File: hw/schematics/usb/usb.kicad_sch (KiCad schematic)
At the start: 4 parts

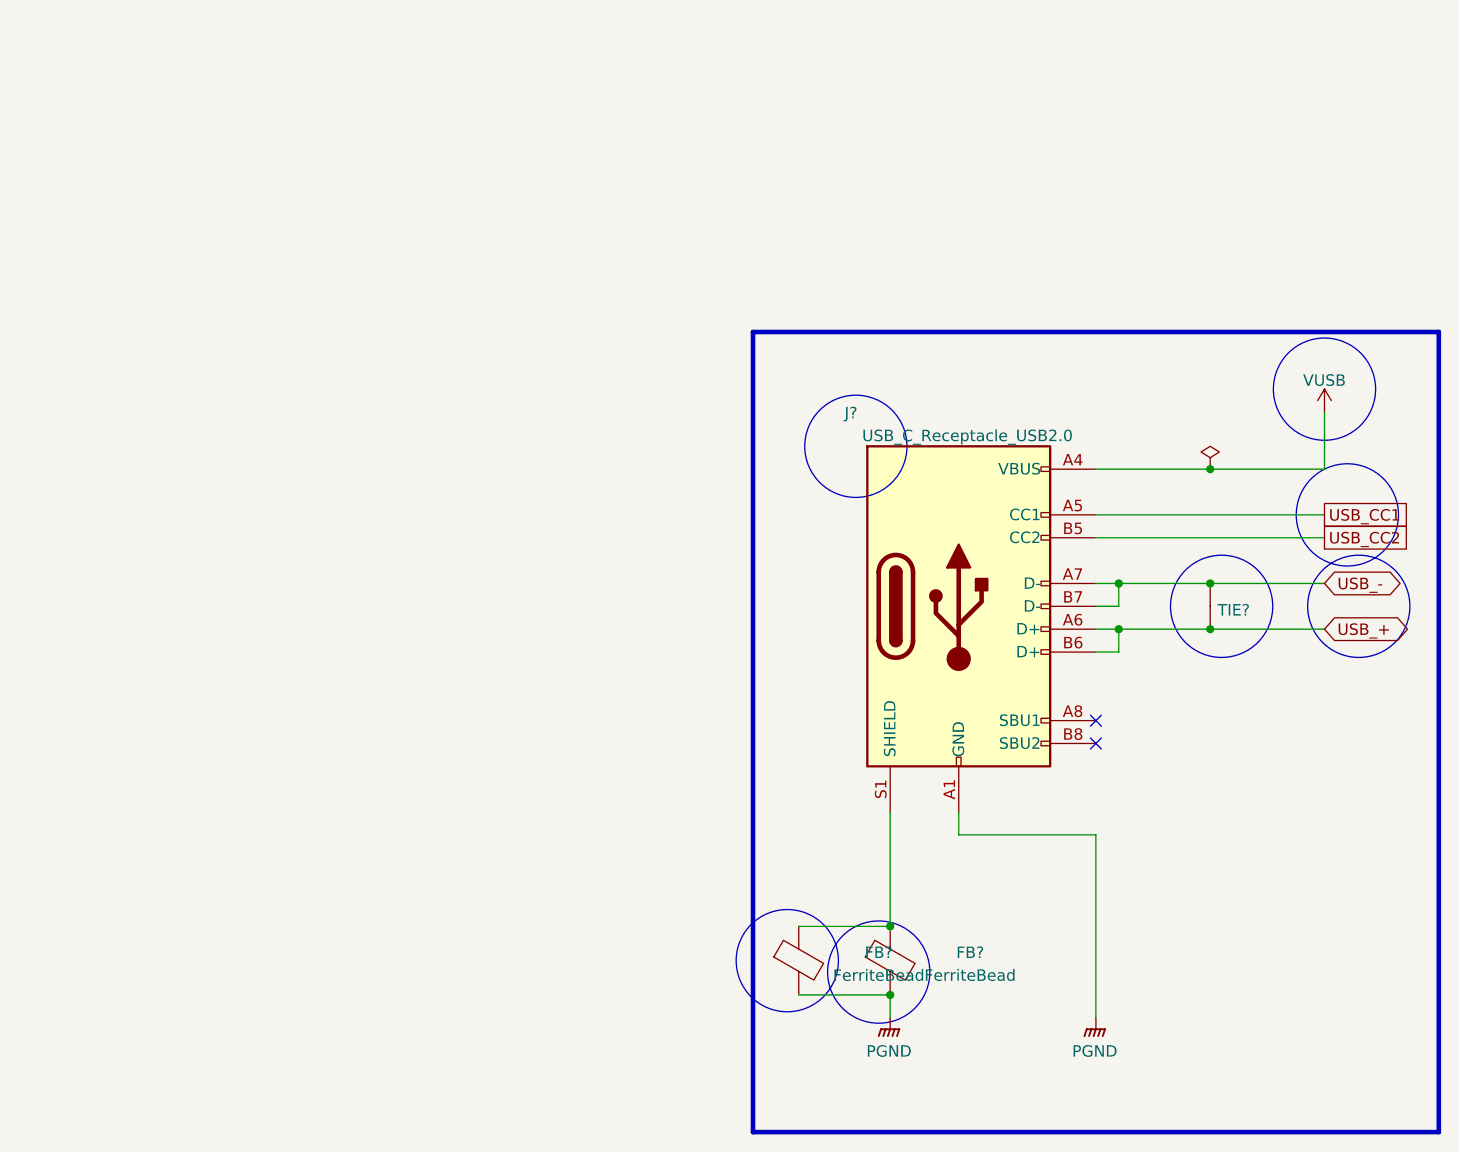
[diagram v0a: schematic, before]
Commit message: 
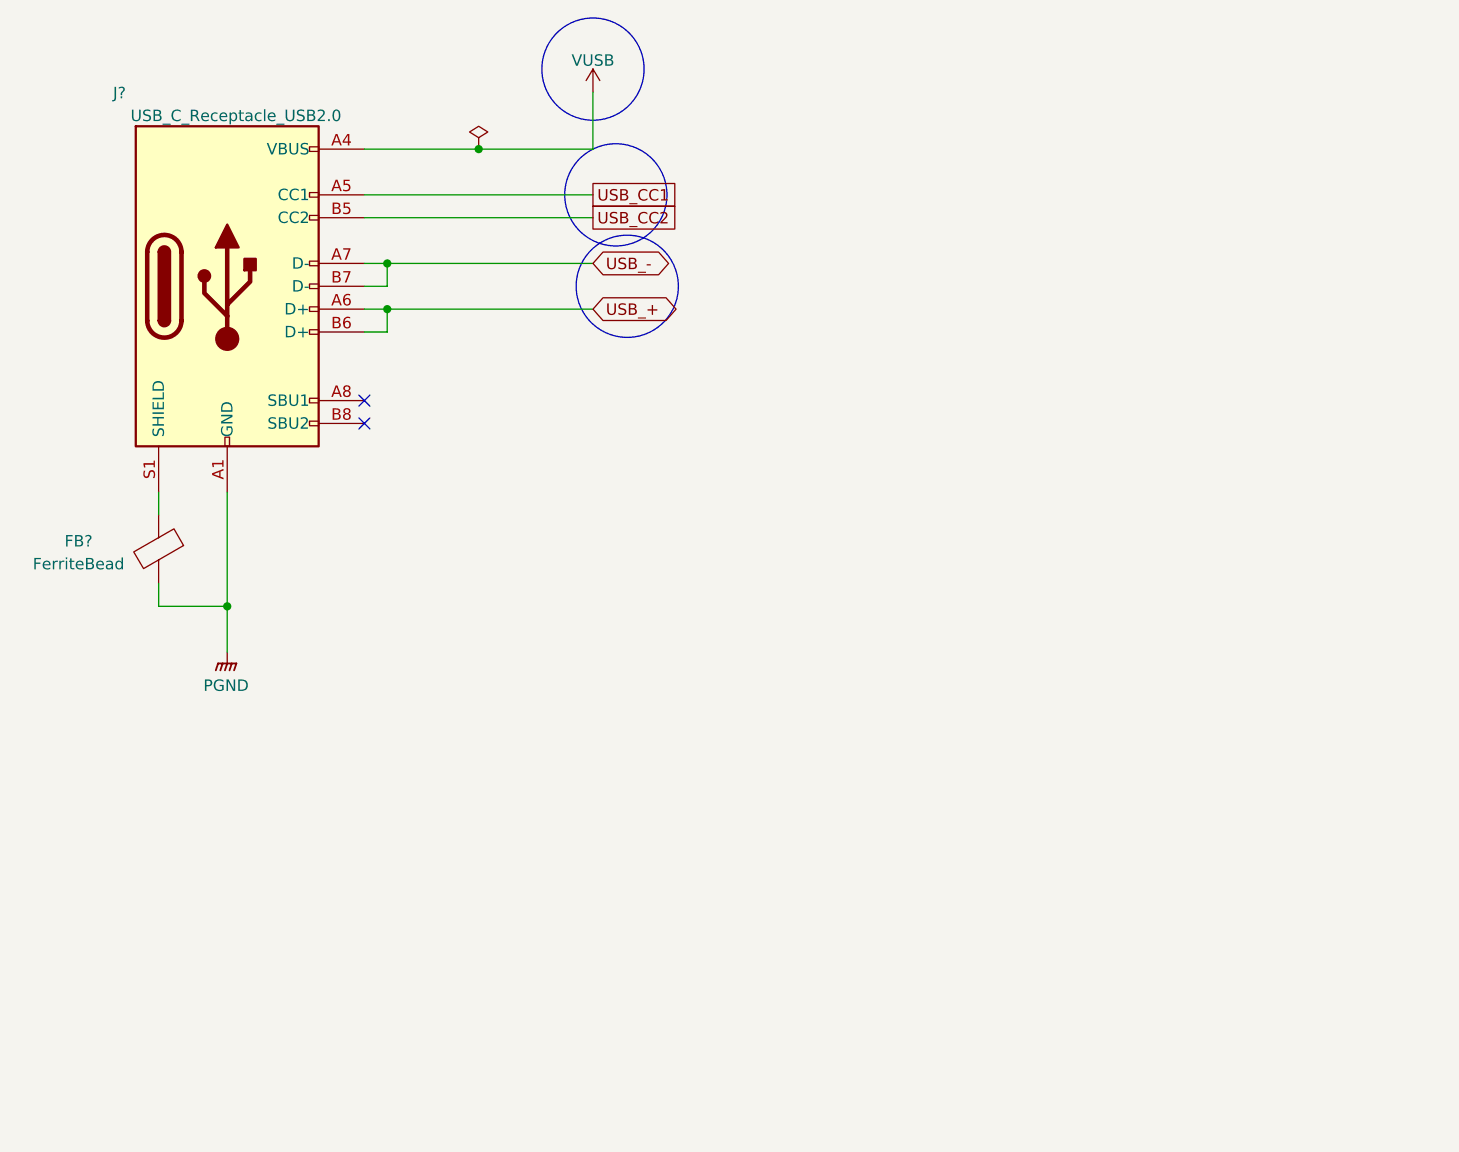
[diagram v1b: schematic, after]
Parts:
- removed FB?: FerriteBead, Resistor_SMD:R_0603_1608Metric, symbol Device:FerriteBead
- removed TIE?: NetTie, 4ms_SolderJumper:Net_Tie_0.16mm_6mil, symbol 4ms_Net-tie:NetTie
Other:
- moved on the sheet: FB?, J?

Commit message: 
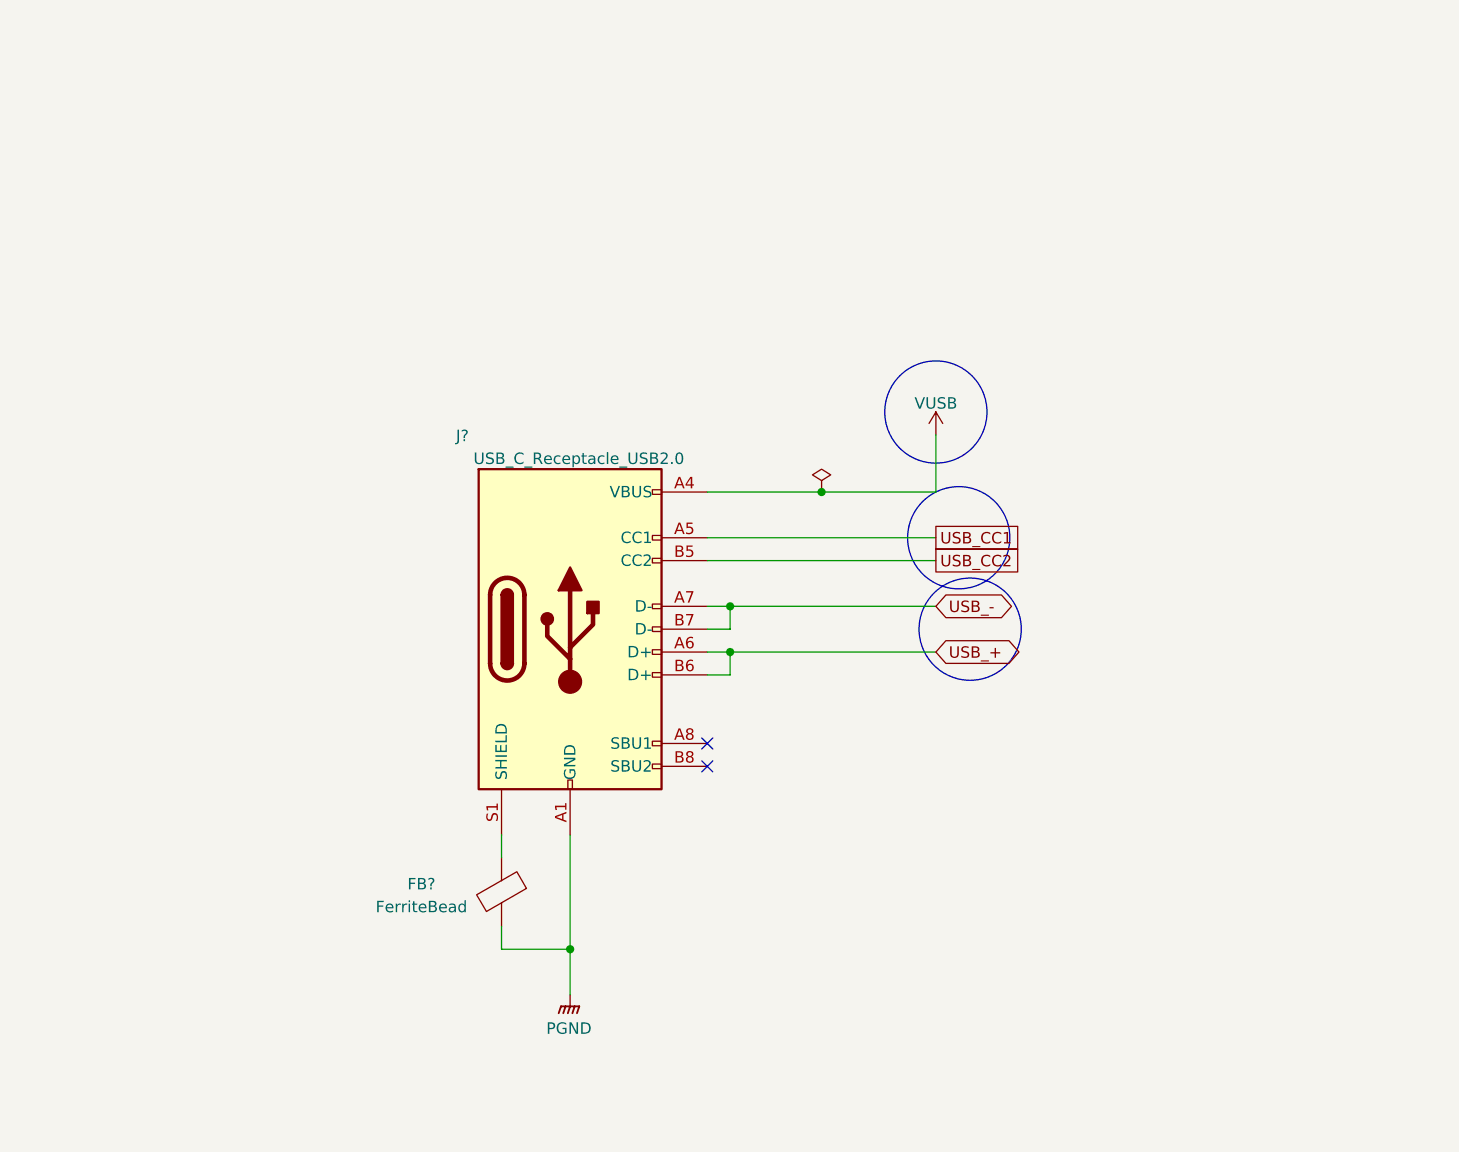
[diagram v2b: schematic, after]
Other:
- moved on the sheet: FB?, J?
